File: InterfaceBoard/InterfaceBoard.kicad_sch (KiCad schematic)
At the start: 0 parts

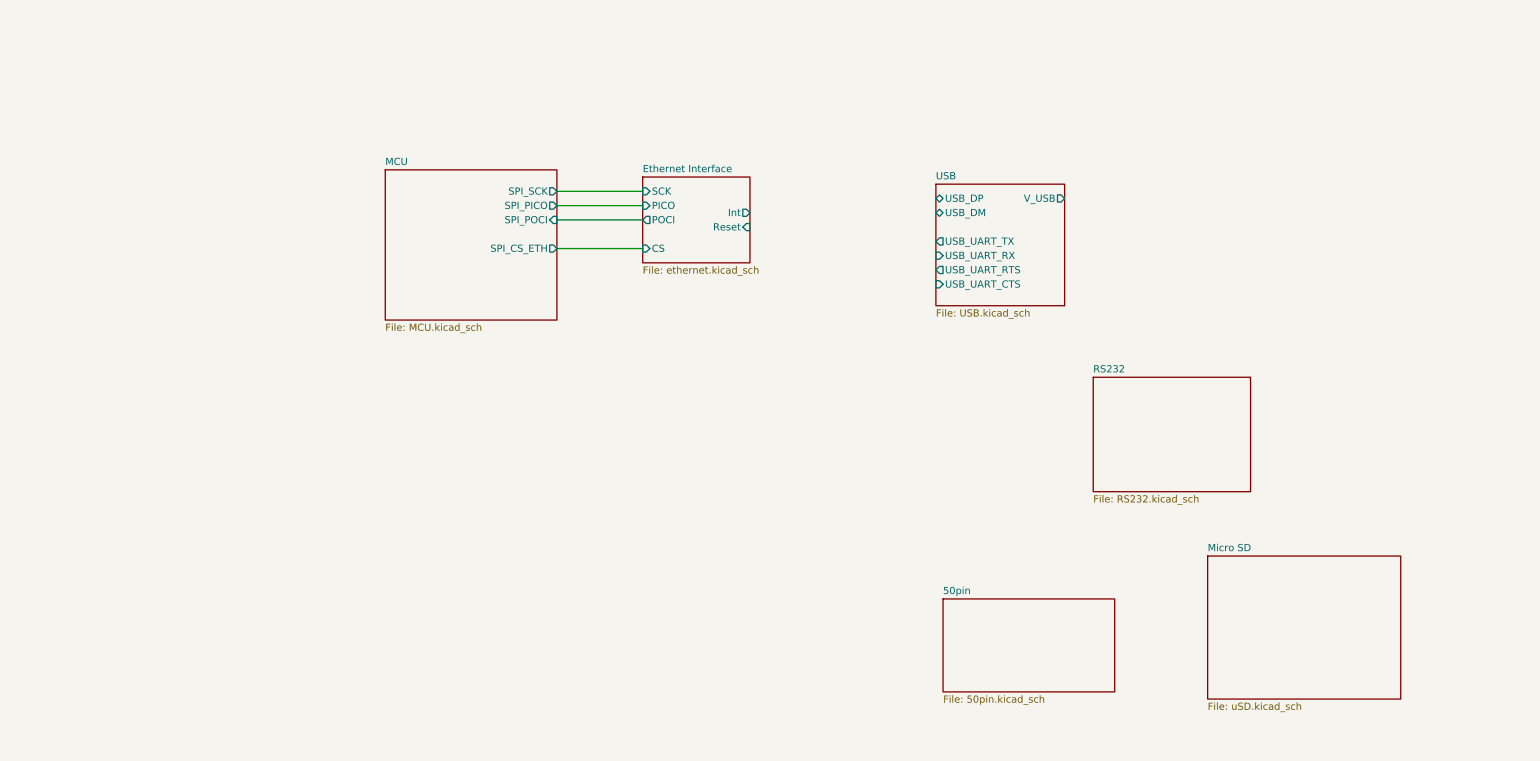
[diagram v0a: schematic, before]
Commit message: InterfaceBoard: Add RS-232/DE-9
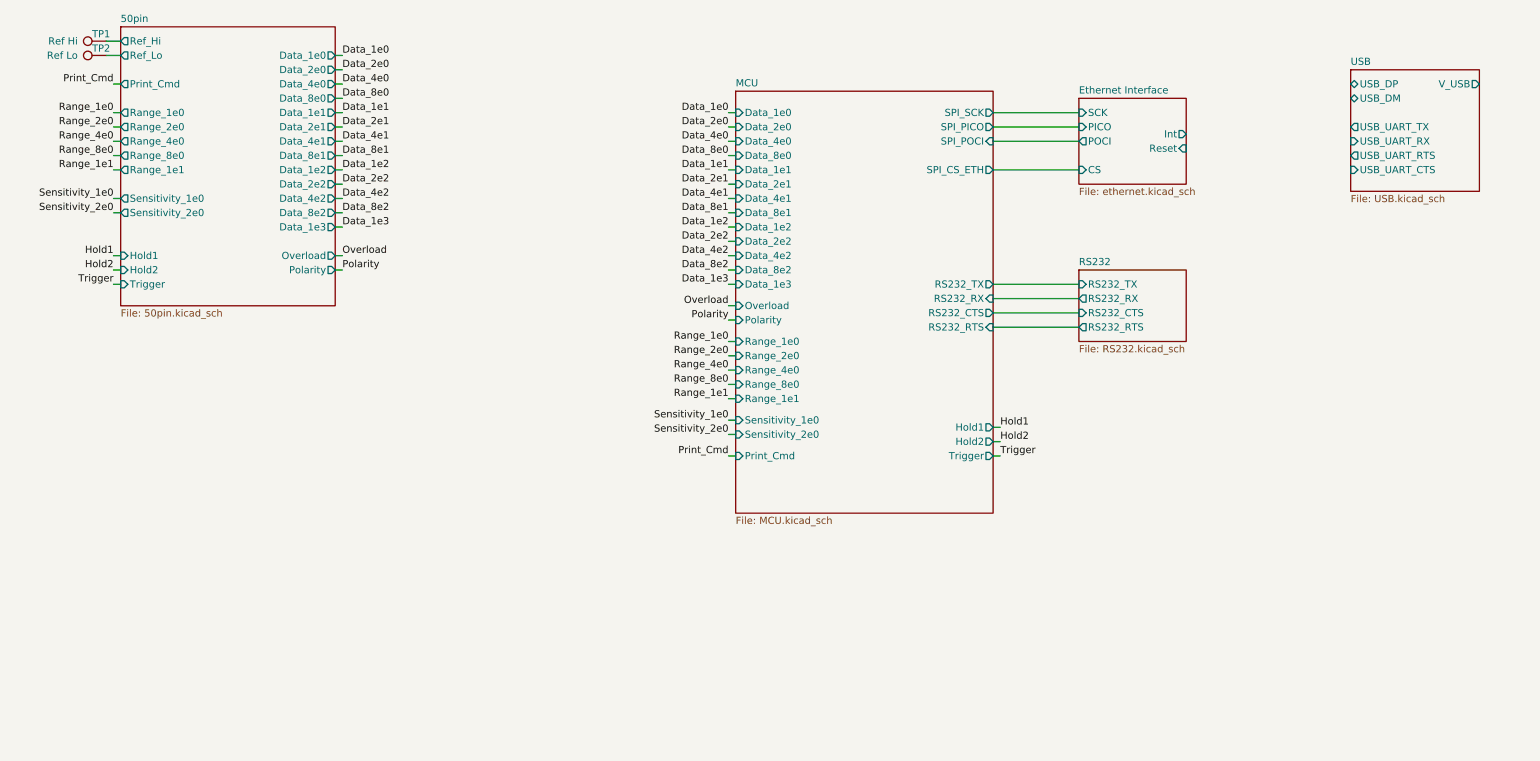
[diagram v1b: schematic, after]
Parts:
- added TP1: Ref Hi, TestPoint:TestPoint_Pad_1.5x1.5mm, symbol Connector:TestPoint
- added TP2: Ref Lo, TestPoint:TestPoint_Pad_1.5x1.5mm, symbol Connector:TestPoint
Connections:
- new net 50pin/Ref_Hi: TP1.1
- new net 50pin/Ref_Lo: TP2.1
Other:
- removed sheet Micro SD
- sheet 50pin ports: added Data_1e0, Data_1e1, Data_1e2, Data_1e3, Data_2e0, Data_2e1, Data_2e2, Data_4e0, Data_4e1, Data_4e2, Data_8e0, Data_8e1, Data_8e2, Hold1, Hold2, Overload, Polarity, Print_Cmd, Range_1e0, Range_1e1, Range_2e0, Range_4e0, Range_8e0, Ref_Hi, Ref_Lo, Sensitivity_1e0, Sensitivity_2e0, Trigger; removed none
- sheet MCU ports: added Data_1e0, Data_1e1, Data_1e2, Data_1e3, Data_2e0, Data_2e1, Data_2e2, Data_4e0, Data_4e1, Data_4e2, Data_8e0, Data_8e1, Data_8e2, Hold1, Hold2, Overload, Polarity, Print_Cmd, RS232_CTS, RS232_RTS, RS232_RX, RS232_TX, Range_1e0, Range_1e1, Range_2e0, Range_4e0, Range_8e0, Sensitivity_1e0, Sensitivity_2e0, Trigger; removed none
- sheet RS232 ports: added RS232_CTS, RS232_RTS, RS232_RX, RS232_TX; removed none

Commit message: InterfaceBoard: Add STM32G0B1RET
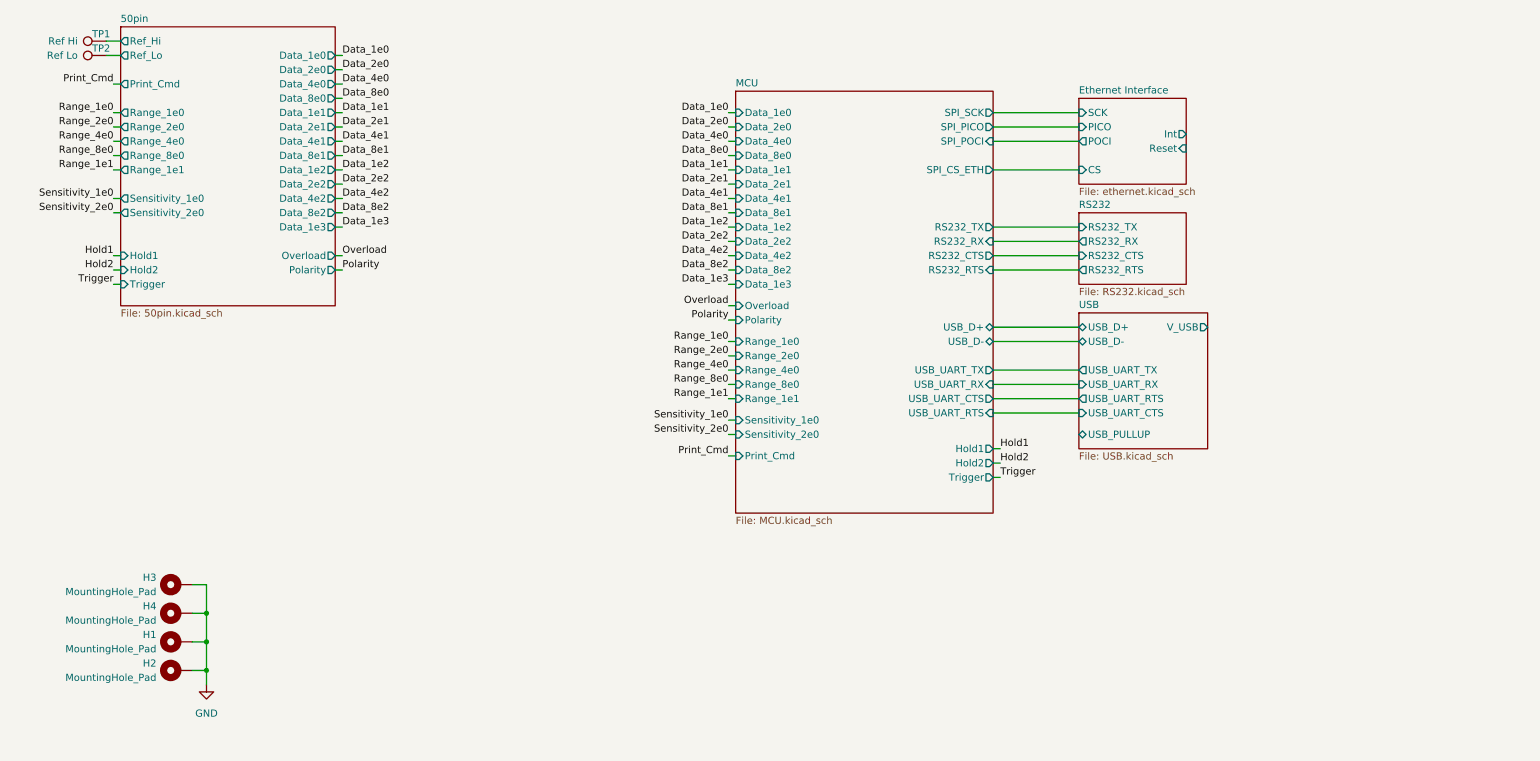
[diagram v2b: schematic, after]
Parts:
- added H1, H2, H3, H4: MountingHole_Pad, MountingHole:MountingHole_3.2mm_M3_Pad, symbol Mechanical:MountingHole_Pad
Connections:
- new net GND: H1.1, H2.1, H3.1, H4.1
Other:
- sheet MCU ports: added USB_D+, USB_D-, USB_UART_CTS, USB_UART_RTS, USB_UART_RX, USB_UART_TX; removed none
- sheet USB ports: added USB_D+, USB_D-, USB_PULLUP; removed USB_DM, USB_DP

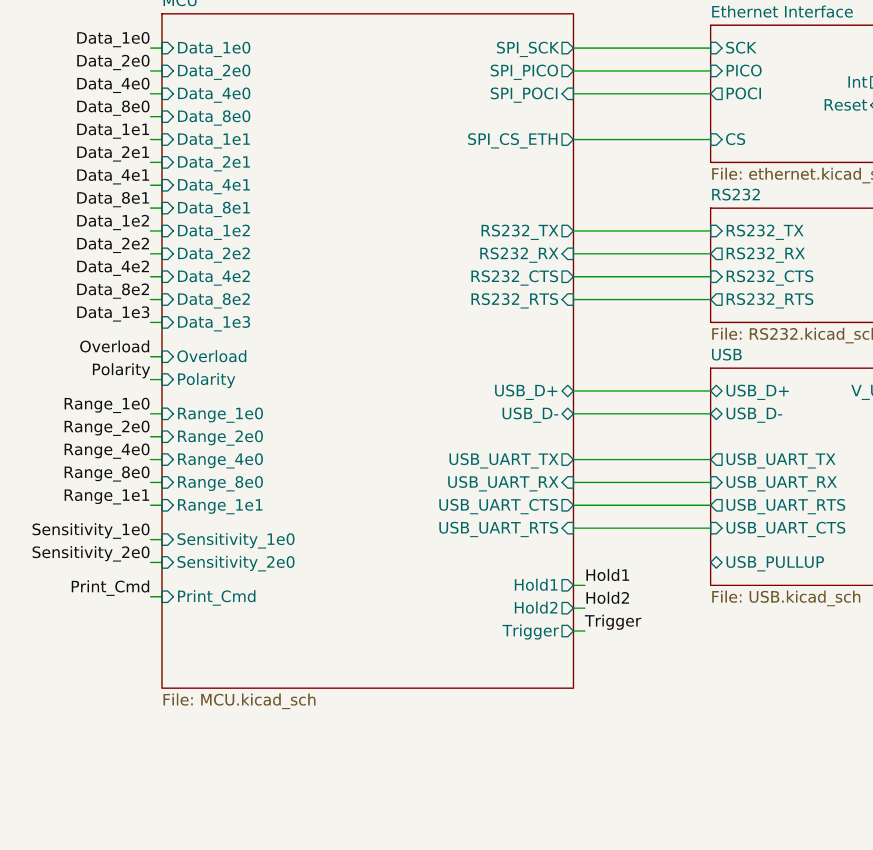
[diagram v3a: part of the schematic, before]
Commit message: InterfaceBoard: Update connector footprint
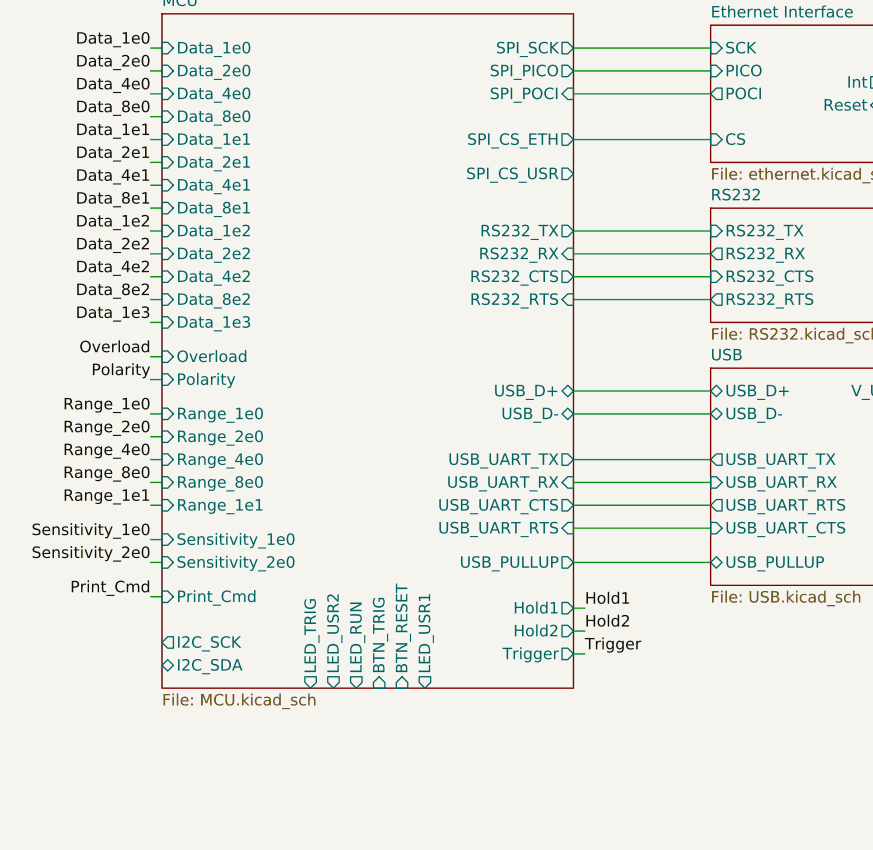
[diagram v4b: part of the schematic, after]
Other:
- sheet MCU ports: added BTN_RESET, BTN_TRIG, I2C_SCK, I2C_SDA, LED_RUN, LED_TRIG, LED_USR1, LED_USR2, SPI_CS_USR, USB_PULLUP; removed none
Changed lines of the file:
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@@
     (stroke (width 0) (type default) (color 0 0 0 0))
   )
-  (wire (pts (xy 185.42 92.71) (xy 184.15 92.71))
+  (wire (pts (xy 185.42 95.25) (xy 184.15 95.25))
     (stroke (width 0) (type default) (color 0 0 0 0))
   )
@@
     (stroke (width 0) (type default) (color 0 0 0 0))
   )
-  (wire (pts (xy 185.42 95.25) (xy 184.15 95.25))
+  (wire (pts (xy 185.42 97.79) (xy 184.15 97.79))
     (stroke (width 0) (type default) (color 0 0 0 0))
   )
@@
     (stroke (width 0) (type default) (color 0 0 0 0))
   )
+  (wire (pts (xy 184.15 90.17) (xy 199.39 90.17))
+    (stroke (width 0) (type default) (color 0 0 0 0))
+  )
   (wire (pts (xy 138.43 40.64) (xy 137.16 40.64))
     (stroke (width 0) (type default) (color 0 0 0 0))
@@
     (stroke (width 0) (type default) (color 0 0 0 0))
   )
-  (wire (pts (xy 185.42 97.79) (xy 184.15 97.79))
+  (wire (pts (xy 185.42 100.33) (xy 184.15 100.33))
     (stroke (width 0) (type default) (color 0 0 0 0))
   )
@@
     (effects (font (size 1.27 1.27)) (justify right bottom))
   )
-  (label "Trigger" (at 185.42 97.79 0)
+  (label "Trigger" (at 185.42 100.33 0)
     (effects (font (size 1.27 1.27)) (justify left bottom))
   )
@@
     (effects (font (size 1.27 1.27)) (justify left bottom))
   )
-  (label "Hold1" (at 185.42 92.71 0)
+  (label "Hold1" (at 185.42 95.25 0)
     (effects (font (size 1.27 1.27)) (justify left bottom))
   )
@@
     (effects (font (size 1.27 1.27)) (justify right bottom))
   )
-  (label "Hold2" (at 185.42 95.25 0)
+  (label "Hold2" (at 185.42 97.79 0)
     (effects (font (size 1.27 1.27)) (justify left bottom))
   )
@@
       (effects (font (size 1.27 1.27)) (justify left))
     )
-    (pin "Hold1" output (at 184.15 92.71 0)
-      (effects (font (size 1.27 1.27)) (justify right))
-    )
-    (pin "Hold2" output (at 184.15 95.25 0)
+    (pin "Hold1" output (at 184.15 95.25 0)
+      (effects (font (size 1.27 1.27)) (justify right))
+    )
+    (pin "Hold2" output (at 184.15 97.79 0)
       (effects (font (size 1.27 1.27)) (justify right))
     )
@@
       (effects (font (size 1.27 1.27)) (justify left))
     )
-    (pin "Trigger" output (at 184.15 97.79 0)
+    (pin "Trigger" output (at 184.15 100.33 0)
       (effects (font (size 1.27 1.27)) (justify right))
     )
@@
     )
     (pin "USB_D-" bidirectional (at 184.15 73.66 0)
+      (effects (font (size 1.27 1.27)) (justify right))
+    )
+    (pin "I2C_SCK" output (at 138.43 99.06 180)
+      (effects (font (size 1.27 1.27)) (justify left))
+    )
+    (pin "I2C_SDA" bidirectional (at 138.43 101.6 180)
+      (effects (font (size 1.27 1.27)) (justify left))
+    )
+    (pin "SPI_CS_USR" output (at 184.15 46.99 0)
+      (effects (font (size 1.27 1.27)) (justify right))
+    )
+    (pin "LED_USR2" output (at 157.48 104.14 270)
+      (effects (font (size 1.27 1.27)) (justify left))
+    )
+    (pin "LED_RUN" output (at 160.02 104.14 270)
+      (effects (font (size 1.27 1.27)) (justify left))
+    )
+    (pin "BTN_TRIG" input (at 162.56 104.14 270)
+      (effects (font (size 1.27 1.27)) (justify left))
+    )
+    (pin "BTN_RESET" input (at 165.1 104.14 270)
+      (effects (font (size 1.27 1.27)) (justify left))
+    )
+    (pin "LED_TRIG" output (at 154.94 104.14 270)
+      (effects (font (size 1.27 1.27)) (justify left))
+    )
+    (pin "LED_USR1" output (at 167.64 104.14 270)
+      (effects (font (size 1.27 1.27)) (justify left))
+    )
+    (pin "USB_PULLUP" output (at 184.15 90.17 0)
       (effects (font (size 1.27 1.27)) (justify right))
     )
@@
     )
     (path "/d012d009-33c3-43a4-bbb3-b4f43de9d077/d6d2fb24-f6fb-4d86-bee6-3937b97a04f8"
-      (reference "#PWR?") (unit 1) (value "+3V3") (footprint "")
+      (reference "#PWR0169") (unit 1) (value "+3V3") (footprint "")
+    )
+    (path "/d012d009-33c3-43a4-bbb3-b4f43de9d077/195b8a57-bba6-4ac4-a80b-374b193dcf00"
+      (reference "#PWR0170") (unit 1) (value "GND") (footprint "")
+    )
+    (path "/d012d009-33c3-43a4-bbb3-b4f43de9d077/75c529aa-1b7b-460c-97af-651f3a6df078"
+      (reference "#PWR0171") (unit 1) (value "GND") (footprint "")
+    )
+    (path "/d012d009-33c3-43a4-bbb3-b4f43de9d077/7db6ac1e-ebd2-485e-8163-cdaeedcb72cf"
+      (reference "#PWR0172") (unit 1) (value "GND") (footprint "")
     )
     (path "/7510d84d-561c-4c04-9a47-602785bf143f/33265ba7-ef1d-49c8-b2f9-33fbd5dfa7c1"
@@
       (reference "C30") (unit 1) (value "100nF") (footprint "Capacitor_SMD:C_0603_1608Metric")
     )
+    (path "/d012d009-33c3-43a4-bbb3-b4f43de9d077/6711e8e8-90b3-486b-9111-6d3049d77b87"
+      (reference "C31") (unit 1) (value "22pF") (footprint "Capacitor_SMD:C_0603_1608Metric")
+    )
+    (path "/d012d009-33c3-43a4-bbb3-b4f43de9d077/fa7ec4c7-d0a5-4110-824e-ab64285707f5"
+      (reference "C32") (unit 1) (value "22pF") (footprint "Capacitor_SMD:C_0603_1608Metric")
+    )
+    (path "/d012d009-33c3-43a4-bbb3-b4f43de9d077/f08fe741-6fac-424b-93e9-aee77344c1d7"
+      (reference "C33") (unit 1) (value "12pF") (footprint "Capacitor_SMD:C_0603_1608Metric")
+    )
+    (path "/d012d009-33c3-43a4-bbb3-b4f43de9d077/5bb0a7c9-98d6-4a65-a0ef-f93e8079102a"
+      (reference "C34") (unit 1) (value "12pF") (footprint "Capacitor_SMD:C_0603_1608Metric")
+    )
     (path "/7510d84d-561c-4c04-9a47-602785bf143f/861607d3-a696-4386-8236-78177bd356d0"
       (reference "D1") (unit 1) (value "Speed") (footprint "LED_SMD:LED_0603_1608Metric")
@@
       (reference "R78") (unit 1) (value "0") (footprint "Resistor_SMD:R_0603_1608Metric")
     )
+    (path "/d012d009-33c3-43a4-bbb3-b4f43de9d077/aa25ec82-24c5-4007-bf88-3618f41d050c"
+      (reference "R79") (unit 1) (value "1.6k") (footprint "Resistor_SMD:R_0603_1608Metric")
+    )
     (path "/6b1005e4-cf6f-4a1d-aca2-678196de2d73"
       (reference "TP1") (unit 1) (value "Ref Hi") (footprint "TestPoint:TestPoint_Pad_1.5x1.5mm")
@@
       (reference "Y1") (unit 1) (value "25 MHz") (footprint "Crystal:Crystal_SMD_3225-4Pin_3.2x2.5mm")
     )
-  )
+    (path "/d012d009-33c3-43a4-bbb3-b4f43de9d077/9bfcac06-2987-4ea0-81bd-f7ee6087e3cc"
+      (reference "Y2") (unit 1) (value "32.768 kHz") (footprint "Crystal:Crystal_C26-LF_D2.1mm_L6.5mm_Horizontal")
+    )
+    (path "/d012d009-33c3-43a4-bbb3-b4f43de9d077/ced345a3-0ffb-43eb-a13c-5023321dfdea"
+      (reference "Y3") (unit 1) (value "24 MHz") (footprint "Crystal:Crystal_SMD_3225-4Pin_3.2x2.5mm")
+    )
+  )
